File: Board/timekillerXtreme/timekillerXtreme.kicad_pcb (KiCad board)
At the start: 2 copper layers, 61.5 x 105.2 mm, 106 parts, among them J1 Battery, J13 CONN_01X03, J15 PE7, J16 PE8, J17 PE9, J18 PE10, J19 PD4, J2 USB_OTG, J20 PD1, J21 PD0, J22 PD3, J23 PE11, J24 Pb12, J3 Conn_Bottom_Expansion, J5 Conn_LCD_Board, J6 uSD, J8 TP_AUDIO_R, J9 TP_AUDIO_L, Q1 IRLML6302, Q2 PMBT3904.215, SW1 PWR, SW2 A, SW3 B, SW4 LEFT, SW5 RIGHT, SW6 DOWN, SW7 UP, SW8 RST, U1 MCP73831, U2 FT230XS-R, U3 NCP1529, U5 STM32F407VGT6, U6 USBLC6, U7 AOZ1310, U8 USBLC6, U9 USBLC6, Y1 32.768 KHz, Y2 16MHz

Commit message: board & schematics updated
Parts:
- removed J15: PE7, Measurement_Points:Measurement_Point_Round-SMD-Pad_Small
- added C14: 2.2u, Capacitors_SMD:C_0805_HandSoldering, B.Cu at (121.2, 78.5)
- added C15: 100n, Capacitors_SMD:C_0805_HandSoldering, B.Cu at (121.2, 76.5)
- added C18: 4.7u, Capacitors_SMD:C_0805_HandSoldering, B.Cu at (124.9, 92.8)
- added C20: 100n, Capacitors_SMD:C_0805_HandSoldering, B.Cu at (167.0, 115.9)
- added C21: 2.2u, Capacitors_SMD:C_0805_HandSoldering, B.Cu at (167.0, 114.0)
- added C24: 100u, Capacitors_SMD:C_1210_HandSoldering, B.Cu at (127.7, 93.7)
- added R24: 10k, Resistors_SMD:R_0805_HandSoldering, B.Cu at (161.7, 81.0)
- added U4: TLV431, TO_SOT_Packages_SMD:TSOT-23, B.Cu at (168.8, 84.3)
- moved C31 38.6 mm to (135.5, 89.3), turned to 270 degrees
- moved J16 7.31 mm to (166.4, 92.0)
- moved J18 6.80 mm to (162.0, 92.0)
- moved J17 6.22 mm to (164.2, 92.0)
- moved C19 1.66 mm to (161.7, 78.6)
- moved C23 1.63 mm to (131.5, 63.4), turned to 270 degrees
- moved C29 1.36 mm to (133.5, 63.4), turned to 270 degrees
- moved C13 0.92 mm to (132.7, 52.8)
- moved C12 0.85 mm to (167.8, 77.4)
- moved D4 0.55 mm to (146.0, 46.8)
- moved C22 0.43 mm to (137.5, 89.3)
- moved R16 0.25 mm to (143.4, 50.3), turned to 180 degrees
- moved SPKR 0.15 mm to (140.6, 45.2)
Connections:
- U5 pad 36: VBUS_SENSE -> 1.2VREF
- U5 pad 38: Net-(J15-Pad1) -> VBUS_SENSE
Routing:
- net Net-(J15-Pad1): track 32.2 -> 0.00 mm
- net 1.2VREF: track 0.00 -> 29.7 mm
- net (no net): track 17.0 -> 0.01 mm, vias 1 -> 0
- net GND: track 463.5 -> 475.0 mm, vias 34 -> 35
- net +3V3: track 492.1 -> 503.3 mm, vias 6 -> 7
- net Net-(R24-Pad2): track 0.00 -> 7.43 mm
- net Net-(J18-Pad1): track 29.6 -> 22.5 mm
- net BTN_0_WKUP: track 71.6 -> 78.3 mm
- net Net-(J17-Pad1): track 29.9 -> 24.4 mm
- net Net-(J16-Pad1): track 31.0 -> 26.0 mm
- net USART2_TX: track 80.1 -> 76.3 mm
- net RESET: track 108.4 -> 106.4 mm, vias 5 -> 4
- net Net-(J23-Pad1): track 20.2 -> 18.9 mm
- net Net-(C12-Pad1): track 27.3 -> 26.3 mm
- net BTN_2_DOWN: track 109.9 -> 108.9 mm
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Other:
- board text added: "Rev. 2 2018-11-04"
- board text removed: "Rev. 1 2018-10-30"

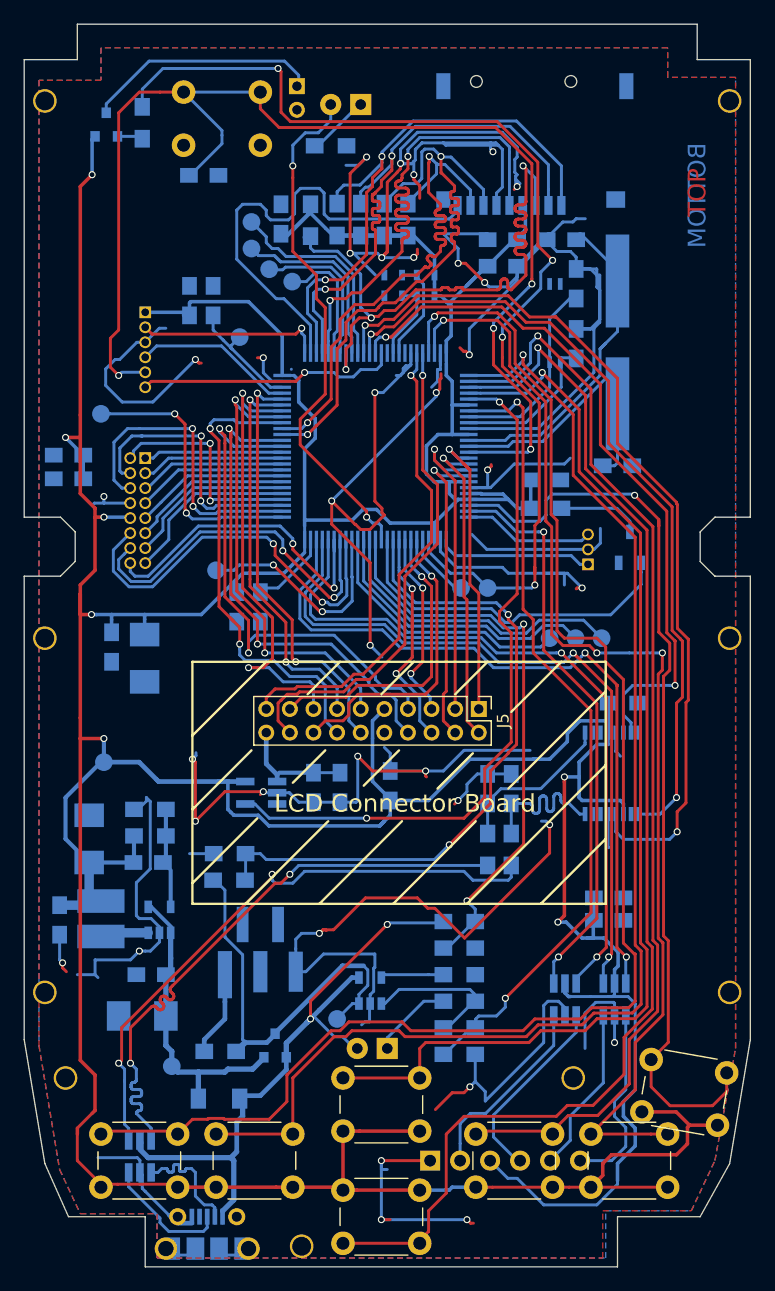
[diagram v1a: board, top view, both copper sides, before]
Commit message: Case and board updated, this will be shipped to the boardhouse and I will call it rev2 if it is ok.
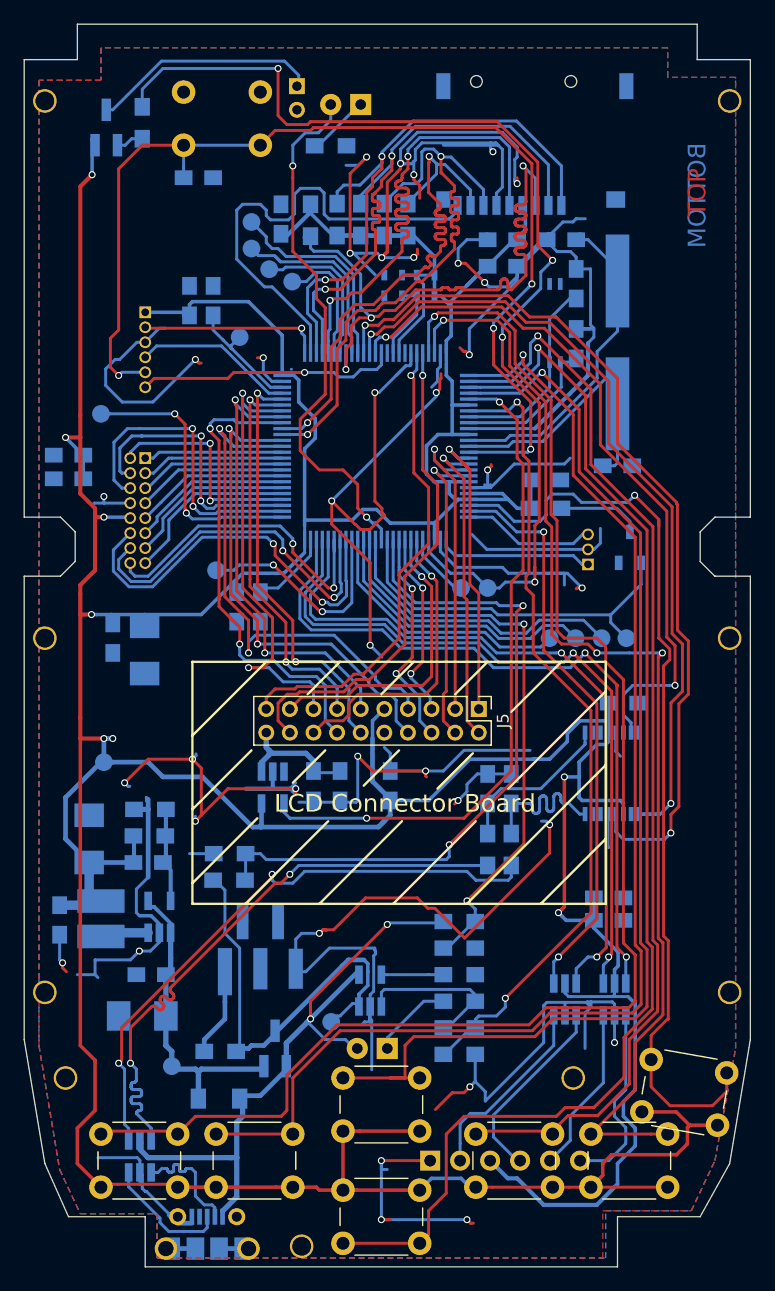
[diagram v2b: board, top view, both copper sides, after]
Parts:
- added VREF: VREF, Measurement_Points:Measurement_Point_Round-SMD-Pad_Small, B.Cu at (168.5, 92.0)
- Q1, Q2: footprint TO_SOT_Packages_SMD:SOT-23 -> TO_SOT_Packages_SMD:SOT-23_Handsoldering
- U1, U3: footprint TO_SOT_Packages_SMD:SOT-23-5 -> TO_SOT_Packages_SMD:SOT-23-5_HandSoldering
- moved SW8 7.91 mm to (137.5, 45.8), turned to 180 degrees
- moved U7 1.07 mm to (138.6, 104.7), turned to 270 degrees
- moved C18 0.76 mm to (125.0, 92.0)
- moved C24 0.70 mm to (127.7, 93.0)
- moved VBATT 0.56 mm to (143.5, 124.5)
- moved C13 0.49 mm to (132.2, 53.0)
- moved U3 0.26 mm to (128.9, 115.6)
- moved J1 0.25 mm to (137.5, 117.8)
- moved Q1 0.25 mm to (138.8, 126.8)
- moved Q2 0.25 mm to (124.5, 48.8)
- moved C32 0.14 mm to (142.0, 104.5)
- moved C33 0.14 mm to (144.2, 104.5)
- moved R8 0.05 mm to (128.1, 108.8)
- renumbered V_USB to VUSB
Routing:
- net RESET: track 106.4 -> 93.7 mm
- net GND: track 475.0 -> 486.5 mm, vias 35 -> 36
- net Net-(C11-Pad1): track 32.2 -> 28.3 mm
- net LCD_BL_SHDN: track 60.3 -> 56.8 mm
- net +3V3: track 503.3 -> 500.2 mm, vias 7 -> 8
- net BTN_1_UP: track 94.3 -> 96.7 mm
- net VBATT_SENSE: track 56.8 -> 59.0 mm
- net BATT+: track 34.9 -> 36.9 mm
- net 1.2VREF: track 29.7 -> 31.7 mm
- net LCD_PWR: track 9.92 -> 11.9 mm
- net USART2_RX: track 67.9 -> 69.8 mm
- net BOARD_REV_DETECT1: track 8.95 -> 10.2 mm
- net USB_VBUS: track 57.7 -> 58.9 mm
- net SYS_LED: track 44.0 -> 45.0 mm
- net Net-(C3-Pad1): track 23.9 -> 24.6 mm
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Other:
- board text added: "Rev. 2 2018-11-14"
- board text added: "solder flat"
- board text removed: "Rev. 2 2018-11-04"

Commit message: Vref fixed, board was sent to boardhouse.
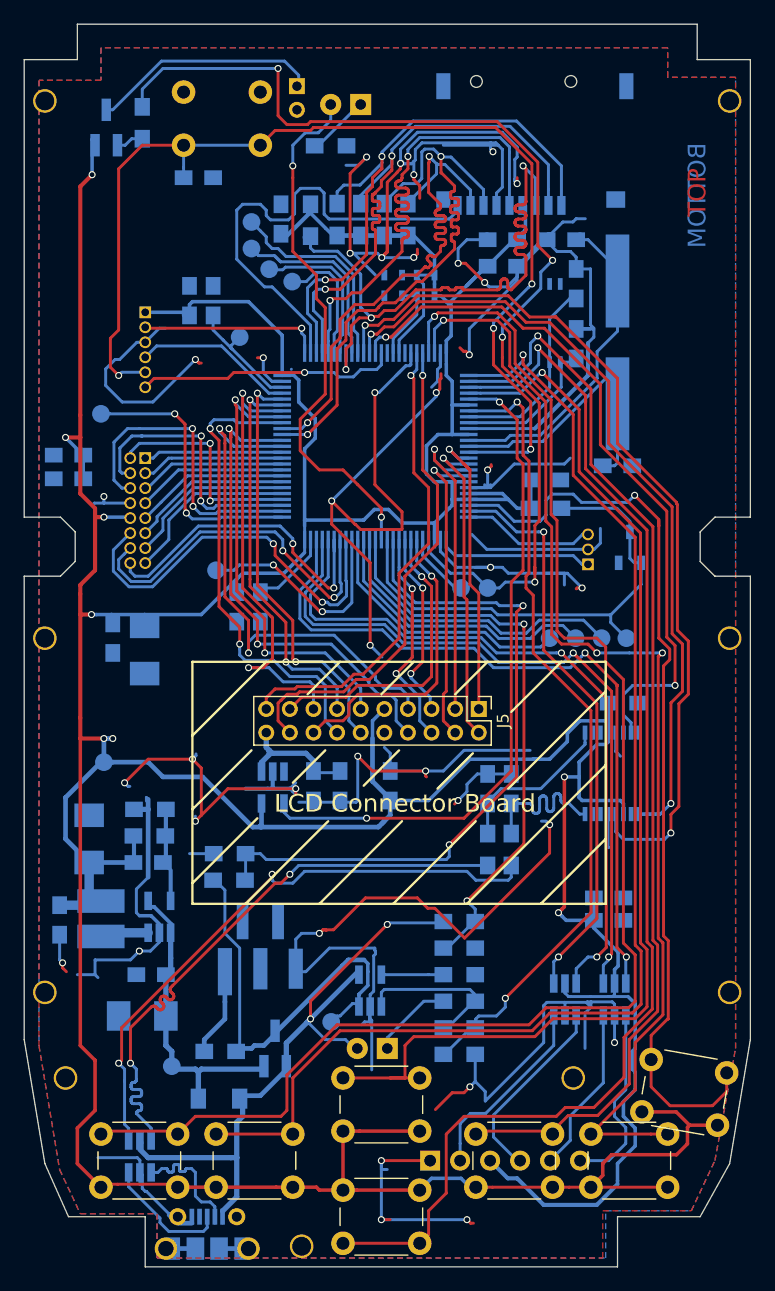
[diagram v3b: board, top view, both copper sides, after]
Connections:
- R24 pad 2: Net-(R24-Pad2) -> 1.2VREF
- U4 pad 3: Net-(R24-Pad2) -> 1.2VREF
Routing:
- net 1.2VREF: track 31.7 -> 42.5 mm
- net Net-(R24-Pad2): track 7.43 -> 0.00 mm
- net GND: track 486.5 -> 490.5 mm, vias 36 -> 37
- net SYS_LED: track 45.0 -> 45.8 mm
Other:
- board text added: "Rev. 2 2018-11-15"
- board text removed: "Rev. 2 2018-11-14"

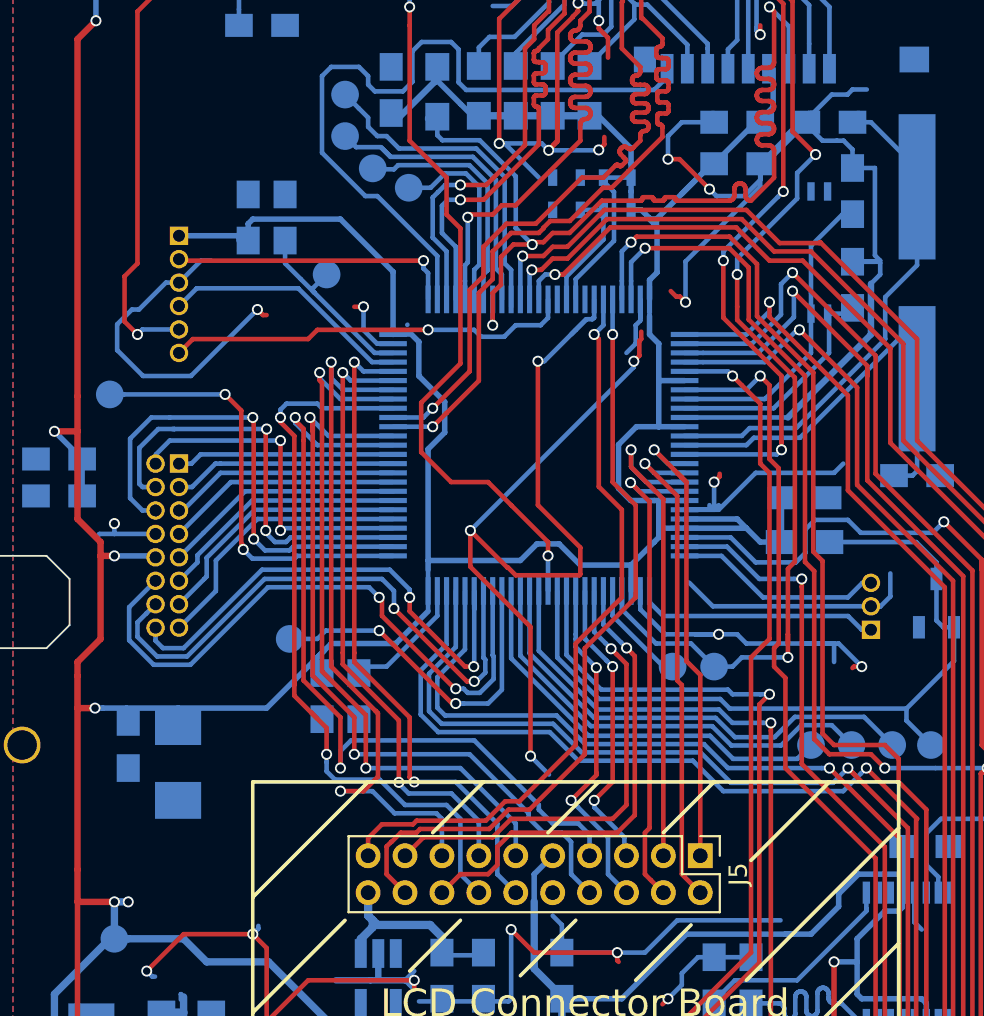
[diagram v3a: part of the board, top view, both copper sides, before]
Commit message: PCB fixes after Rev2 assembly, new assembly docs added.
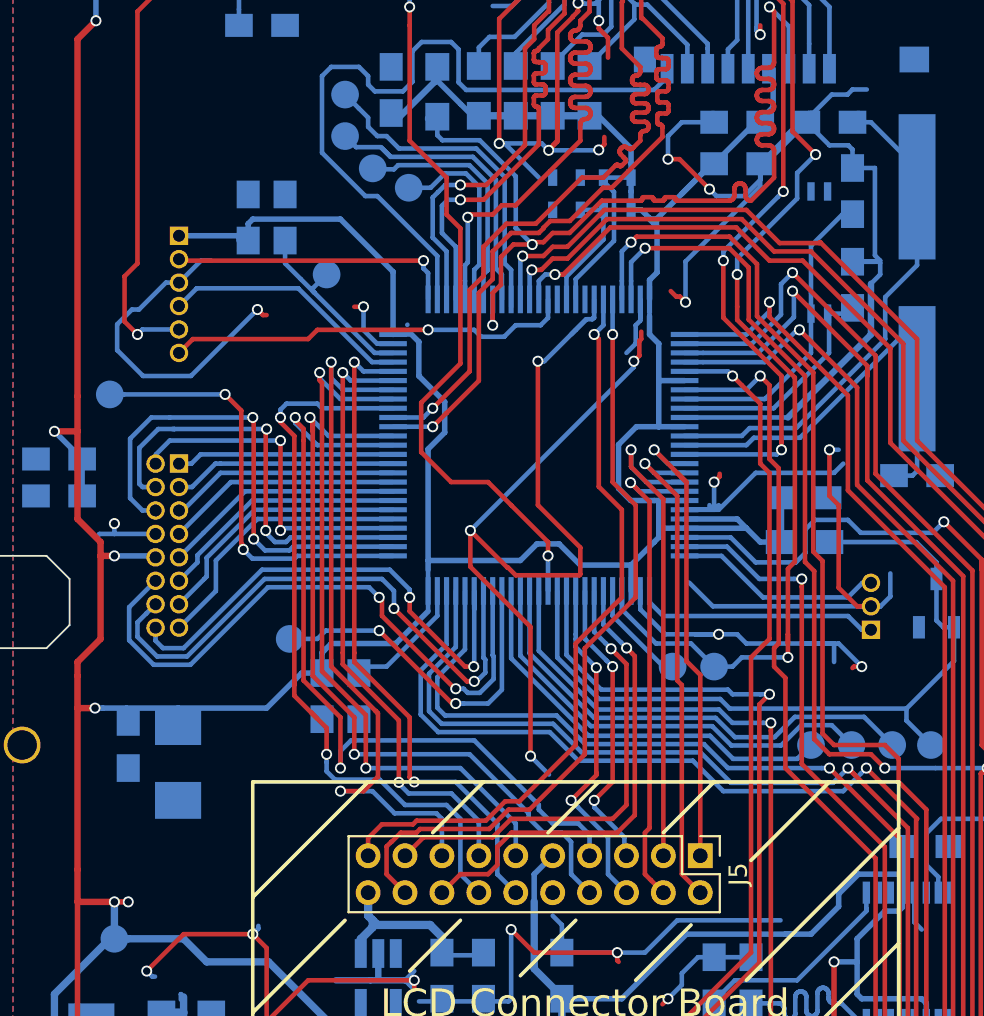
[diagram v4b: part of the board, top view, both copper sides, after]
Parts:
- VCAP: value CAPTEST -> VCAP
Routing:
- net GND: track 490.5 -> 500.8 mm, vias 37 -> 38
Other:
- board text added: "L1"
- board text added: "Rev Detect"
- board text added: "Rev. 2b 2018-11-23"
- board text added: "X7R"
- board text removed: "Rev. 2 2018-11-15"
